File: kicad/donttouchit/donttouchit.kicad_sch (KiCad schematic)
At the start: 46 parts, among them J1 Conn_01x02_Female, J10 Conn_01x04_Male, J2 Conn_01x02_Female, J3 Conn_01x02_Female, J4 Conn_01x02_Female, J5 Conn_01x02_Female, J6 Conn_01x02_Female, J7 Conn_01x02_Female, J8 Conn_01x02_Female, J9 Conn_01x02_Female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

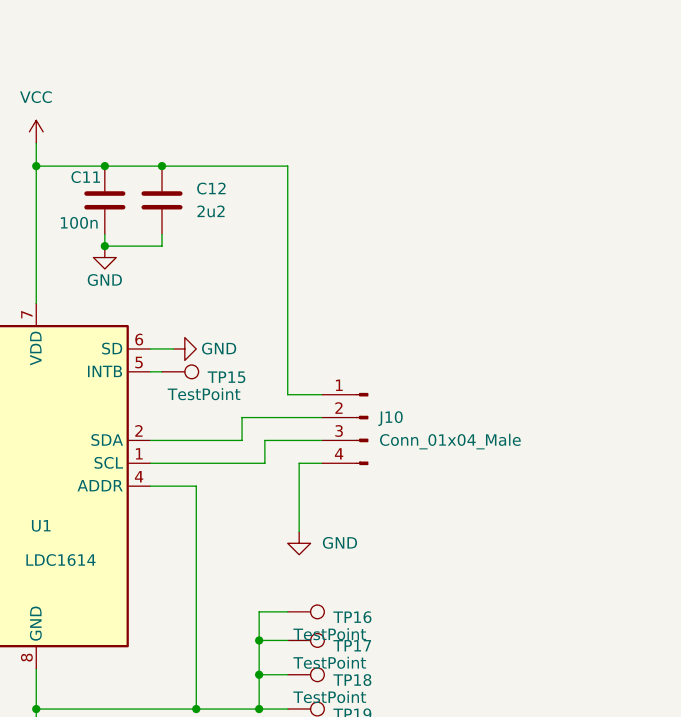
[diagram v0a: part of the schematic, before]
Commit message: i2c pull up resistors added
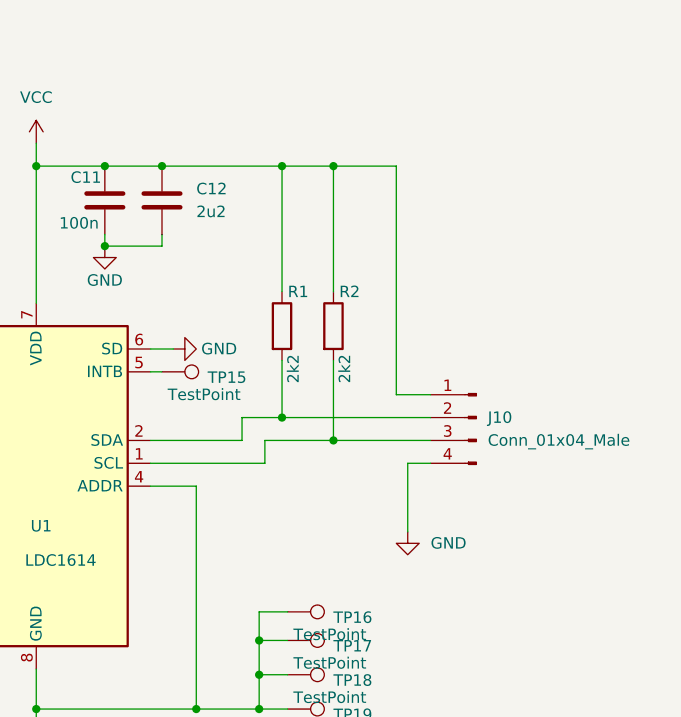
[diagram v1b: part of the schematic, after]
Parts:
- added R1, R2: 2k2, Resistor_SMD:R_0603_1608Metric_Pad0.98x0.95mm_HandSolder, symbol Device:R
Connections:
- net VCC: now also R1.1, R2.1
- net at J10.3 (Pin_3), U1.1 (SCL): now also R2.2
- net at J10.2 (Pin_2), U1.2 (SDA): now also R1.2
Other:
- moved on the sheet: J10
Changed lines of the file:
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@@
   (junction (at 57.785 93.98) (diameter 0) (color 0 0 0 0)
   )
+  (junction (at 204.47 75.565) (diameter 0) (color 0 0 0 0)
+  )
   (junction (at 57.785 115.57) (diameter 0) (color 0 0 0 0)
   )
+  (junction (at 198.755 75.565) (diameter 0) (color 0 0 0 0)
+  )
   (junction (at 57.785 104.775) (diameter 0) (color 0 0 0 0)
   )
@@
   (junction (at 134.62 100.965) (diameter 0) (color 0 0 0 0)
   )
+  (junction (at 198.755 103.505) (diameter 0) (color 0 0 0 0)
+  )
   (junction (at 107.95 103.505) (diameter 0) (color 0 0 0 0)
   )
@@
   (junction (at 179.07 84.455) (diameter 0) (color 0 0 0 0)
   )
+  (junction (at 204.47 106.045) (diameter 0) (color 0 0 0 0)
+  )
   (wire (pts (xy 93.345 110.49) (xy 93.345 113.665))
     (stroke (width 0) (type default) (color 0 0 0 0))
@@
     (stroke (width 0) (type default) (color 0 0 0 0))
   )
+  (wire (pts (xy 198.755 75.565) (xy 204.47 75.565))
+    (stroke (width 0) (type default) (color 0 0 0 0))
+  )
   (wire (pts (xy 196.215 132.08) (xy 196.215 135.89))
     (stroke (width 0) (type default) (color 0 0 0 0))
@@
     (stroke (width 0) (type default) (color 0 0 0 0))
   )
+  (wire (pts (xy 204.47 97.155) (xy 204.47 106.045))
+    (stroke (width 0) (type default) (color 0 0 0 0))
+  )
   (wire (pts (xy 50.8 115.57) (xy 50.8 116.205))
     (stroke (width 0) (type default) (color 0 0 0 0))
@@
     (stroke (width 0) (type default) (color 0 0 0 0))
   )
-  (wire (pts (xy 194.31 103.505) (xy 203.2 103.505))
+  (wire (pts (xy 194.31 103.505) (xy 198.755 103.505))
     (stroke (width 0) (type default) (color 0 0 0 0))
   )
@@
     (stroke (width 0) (type default) (color 0 0 0 0))
   )
-  (wire (pts (xy 199.39 75.565) (xy 199.39 100.965))
+  (wire (pts (xy 211.455 75.565) (xy 211.455 100.965))
     (stroke (width 0) (type default) (color 0 0 0 0))
   )
@@
     (stroke (width 0) (type default) (color 0 0 0 0))
   )
-  (wire (pts (xy 199.39 100.965) (xy 203.2 100.965))
+  (wire (pts (xy 211.455 100.965) (xy 215.265 100.965))
     (stroke (width 0) (type default) (color 0 0 0 0))
   )
@@
     (stroke (width 0) (type default) (color 0 0 0 0))
   )
-  (wire (pts (xy 203.2 108.585) (xy 200.66 108.585))
+  (wire (pts (xy 215.265 108.585) (xy 212.725 108.585))
     (stroke (width 0) (type default) (color 0 0 0 0))
   )
@@
     (stroke (width 0) (type default) (color 0 0 0 0))
   )
+  (wire (pts (xy 198.755 75.565) (xy 198.755 89.535))
+    (stroke (width 0) (type default) (color 0 0 0 0))
+  )
   (wire (pts (xy 73.025 100.33) (xy 73.025 103.505))
     (stroke (width 0) (type default) (color 0 0 0 0))
   )
-  (wire (pts (xy 185.42 75.565) (xy 199.39 75.565))
+  (wire (pts (xy 198.755 97.155) (xy 198.755 103.505))
     (stroke (width 0) (type default) (color 0 0 0 0))
   )
@@
     (stroke (width 0) (type default) (color 0 0 0 0))
   )
+  (wire (pts (xy 204.47 75.565) (xy 204.47 89.535))
+    (stroke (width 0) (type default) (color 0 0 0 0))
+  )
   (wire (pts (xy 134.62 56.515) (xy 139.7 56.515))
     (stroke (width 0) (type default) (color 0 0 0 0))
@@
     (stroke (width 0) (type default) (color 0 0 0 0))
   )
+  (wire (pts (xy 204.47 106.045) (xy 215.265 106.045))
+    (stroke (width 0) (type default) (color 0 0 0 0))
+  )
   (wire (pts (xy 100.965 93.98) (xy 100.965 97.155))
     (stroke (width 0) (type default) (color 0 0 0 0))
@@
     (stroke (width 0) (type default) (color 0 0 0 0))
   )
+  (wire (pts (xy 204.47 75.565) (xy 211.455 75.565))
+    (stroke (width 0) (type default) (color 0 0 0 0))
+  )
   (wire (pts (xy 82.55 115.57) (xy 73.66 115.57))
     (stroke (width 0) (type default) (color 0 0 0 0))
@@
     (stroke (width 0) (type default) (color 0 0 0 0))
   )
+  (wire (pts (xy 198.755 103.505) (xy 215.265 103.505))
+    (stroke (width 0) (type default) (color 0 0 0 0))
+  )
   (wire (pts (xy 107.315 121.285) (xy 107.315 124.46))
     (stroke (width 0) (type default) (color 0 0 0 0))
@@
     (stroke (width 0) (type default) (color 0 0 0 0))
   )
+  (wire (pts (xy 185.42 75.565) (xy 198.755 75.565))
+    (stroke (width 0) (type default) (color 0 0 0 0))
+  )
   (wire (pts (xy 140.97 118.745) (xy 144.78 118.745))
     (stroke (width 0) (type default) (color 0 0 0 0))
@@
     (stroke (width 0) (type default) (color 0 0 0 0))
   )
-  (wire (pts (xy 200.66 108.585) (xy 200.66 116.205))
+  (wire (pts (xy 212.725 108.585) (xy 212.725 116.205))
     (stroke (width 0) (type default) (color 0 0 0 0))
   )
@@
     (stroke (width 0) (type default) (color 0 0 0 0))
   )
-  (wire (pts (xy 196.85 106.045) (xy 203.2 106.045))
+  (wire (pts (xy 196.85 106.045) (xy 204.47 106.045))
     (stroke (width 0) (type default) (color 0 0 0 0))
   )
@@
     (pin "1")
   )
+  (symbol (lib_id "Device:R") (at 198.755 93.345 0) (unit 1)
+    (in_bom yes) (on_board yes)
+    (property "Reference" "R1" (id 0) (at 199.39 89.535 0)
+      (effects (font (size 1.27 1.27)) (justify left))
+    )
+    (property "Value" "2k2" (id 1) (at 200.025 99.695 90)
+      (effects (font (size 1.27 1.27)) (justify left))
+    )
+    (property "Footprint" "Resistor_SMD:R_0603_1608Metric_Pad0.98x0.95mm_HandSolder" (id 2) (at 196.977 93.345 90)
+      (effects (font (size 1.27 1.27)) hide)
+    )
+    (property "Datasheet" "~" (id 3) (at 198.755 93.345 0)
+      (effects (font (size 1.27 1.27)) hide)
+    )
+    (pin "1")
+    (pin "2")
+  )
   (symbol (lib_id "Connector:TestPoint") (at 185.42 98.425 270) (unit 1)
     (in_bom yes) (on_board yes)
@@
     (pin "2")
   )
-  (symbol (lib_id "power:GND") (at 200.66 116.205 0) (mirror y) (unit 1)
-    (in_bom yes) (on_board yes) (fields_autoplaced)
-    (property "Reference" "#PWR09" (id 0) (at 200.66 122.555 0)
-      (effects (font (size 1.27 1.27)) hide)
-    )
-    (property "Value" "GND" (id 1) (at 203.2 117.4749 0)
+  (symbol (lib_id "power:GND") (at 212.725 116.205 0) (mirror y) (unit 1)
+    (in_bom yes) (on_board yes) (fields_autoplaced)
+    (property "Reference" "#PWR09" (id 0) (at 212.725 122.555 0)
+      (effects (font (size 1.27 1.27)) hide)
+    )
+    (property "Value" "GND" (id 1) (at 215.265 117.4749 0)
       (effects (font (size 1.27 1.27)) (justify right))
     )
-    (property "Footprint" "" (id 2) (at 200.66 116.205 0)
-      (effects (font (size 1.27 1.27)) hide)
-    )
-    (property "Datasheet" "" (id 3) (at 200.66 116.205 0)
+    (property "Footprint" "" (id 2) (at 212.725 116.205 0)
+      (effects (font (size 1.27 1.27)) hide)
+    )
+    (property "Datasheet" "" (id 3) (at 212.725 116.205 0)
       (effects (font (size 1.27 1.27)) hide)
     )
@@
     (pin "1")
   )
-  (symbol (lib_id "Connector:Conn_01x04_Male") (at 208.28 103.505 0) (mirror y) (unit 1)
-    (in_bom yes) (on_board yes) (fields_autoplaced)
-    (property "Reference" "J10" (id 0) (at 209.55 103.5049 0)
+  (symbol (lib_id "Connector:Conn_01x04_Male") (at 220.345 103.505 0) (mirror y) (unit 1)
+    (in_bom yes) (on_board yes) (fields_autoplaced)
+    (property "Reference" "J10" (id 0) (at 221.615 103.5049 0)
       (effects (font (size 1.27 1.27)) (justify right))
     )
-    (property "Value" "Conn_01x04_Male" (id 1) (at 209.55 106.0449 0)
+    (property "Value" "Conn_01x04_Male" (id 1) (at 221.615 106.0449 0)
       (effects (font (size 1.27 1.27)) (justify right))
     )
-    (property "Footprint" "Connector_JST:JST_PH_B4B-PH-SM4-TB_1x04-1MP_P2.00mm_Vertical" (id 2) (at 208.28 103.505 0)
-      (effects (font (size 1.27 1.27)) hide)
-    )
-    (property "Datasheet" "~" (id 3) (at 208.28 103.505 0)
+    (property "Footprint" "Connector_JST:JST_PH_B4B-PH-SM4-TB_1x04-1MP_P2.00mm_Vertical" (id 2) (at 220.345 103.505 0)
+      (effects (font (size 1.27 1.27)) hide)
+    )
+    (property "Datasheet" "~" (id 3) (at 220.345 103.505 0)
       (effects (font (size 1.27 1.27)) hide)
     )
@@
     (pin "1")
   )
+  (symbol (lib_id "Device:R") (at 204.47 93.345 0) (unit 1)
+    (in_bom yes) (on_board yes)
+    (property "Reference" "R2" (id 0) (at 205.105 89.535 0)
+      (effects (font (size 1.27 1.27)) (justify left))
+    )
+    (property "Value" "2k2" (id 1) (at 205.74 99.695 90)
+      (effects (font (size 1.27 1.27)) (justify left))
+    )
+    (property "Footprint" "Resistor_SMD:R_0603_1608Metric_Pad0.98x0.95mm_HandSolder" (id 2) (at 202.692 93.345 90)
+      (effects (font (size 1.27 1.27)) hide)
+    )
+    (property "Datasheet" "~" (id 3) (at 204.47 93.345 0)
+      (effects (font (size 1.27 1.27)) hide)
+    )
+    (pin "1")
+    (pin "2")
+  )
   (symbol (lib_id "power:GND") (at 134.62 85.725 0) (unit 1)
     (in_bom yes) (on_board yes) (fields_autoplaced)
@@
       (reference "L3") (unit 1) (value "PCB Coil") (footprint "Library:Coil")
     )
+    (path "/39624e1f-8c52-44d2-9675-d08e055559ed"
+      (reference "R1") (unit 1) (value "2k2") (footprint "Resistor_SMD:R_0603_1608Metric_Pad0.98x0.95mm_HandSolder")
+    )
+    (path "/f0806e7c-4b6c-4326-bfd0-53fcb69c9d00"
+      (reference "R2") (unit 1) (value "2k2") (footprint "Resistor_SMD:R_0603_1608Metric_Pad0.98x0.95mm_HandSolder")
+    )
     (path "/ea8f5060-c83f-4b39-9e48-2e7638c5ee62"

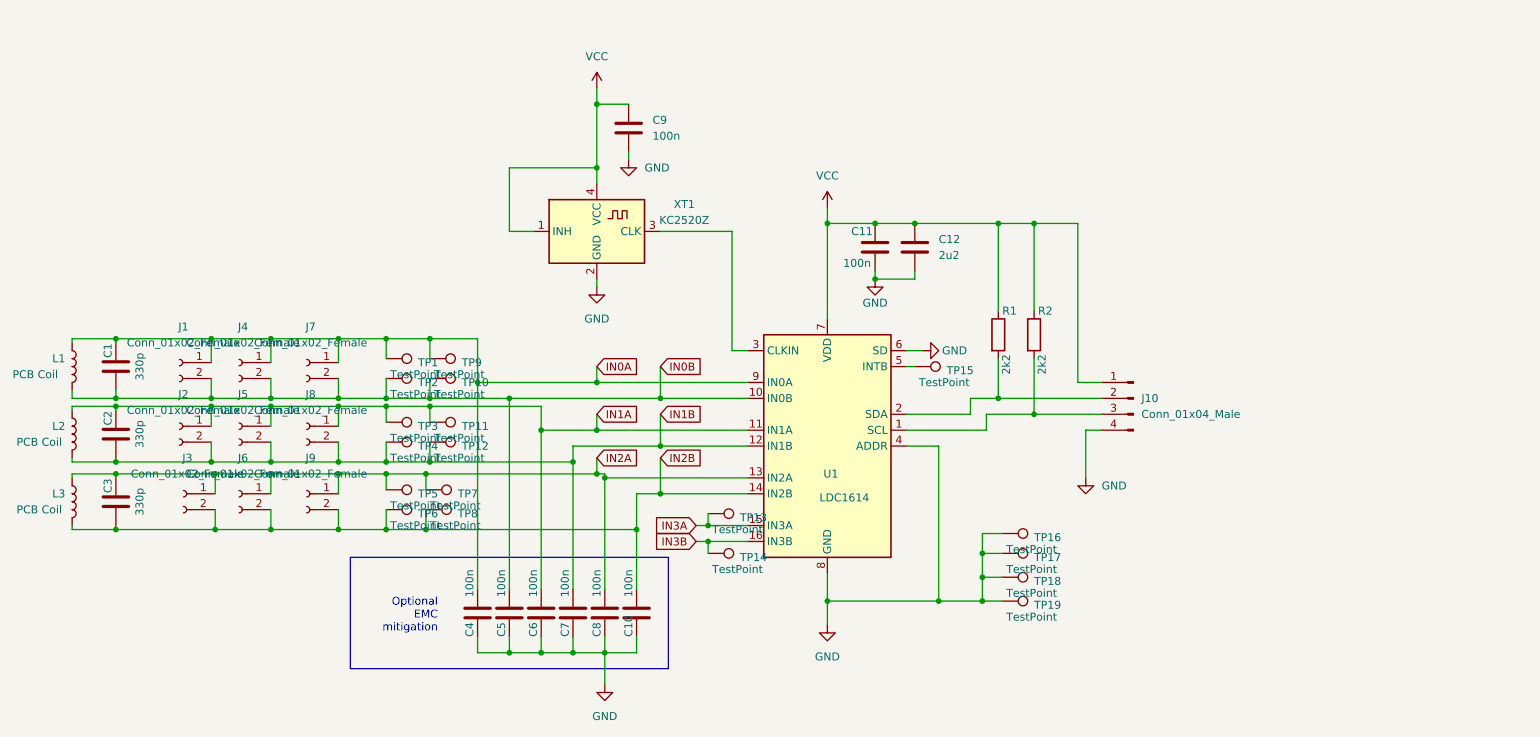
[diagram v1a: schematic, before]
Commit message: temperature sensor added
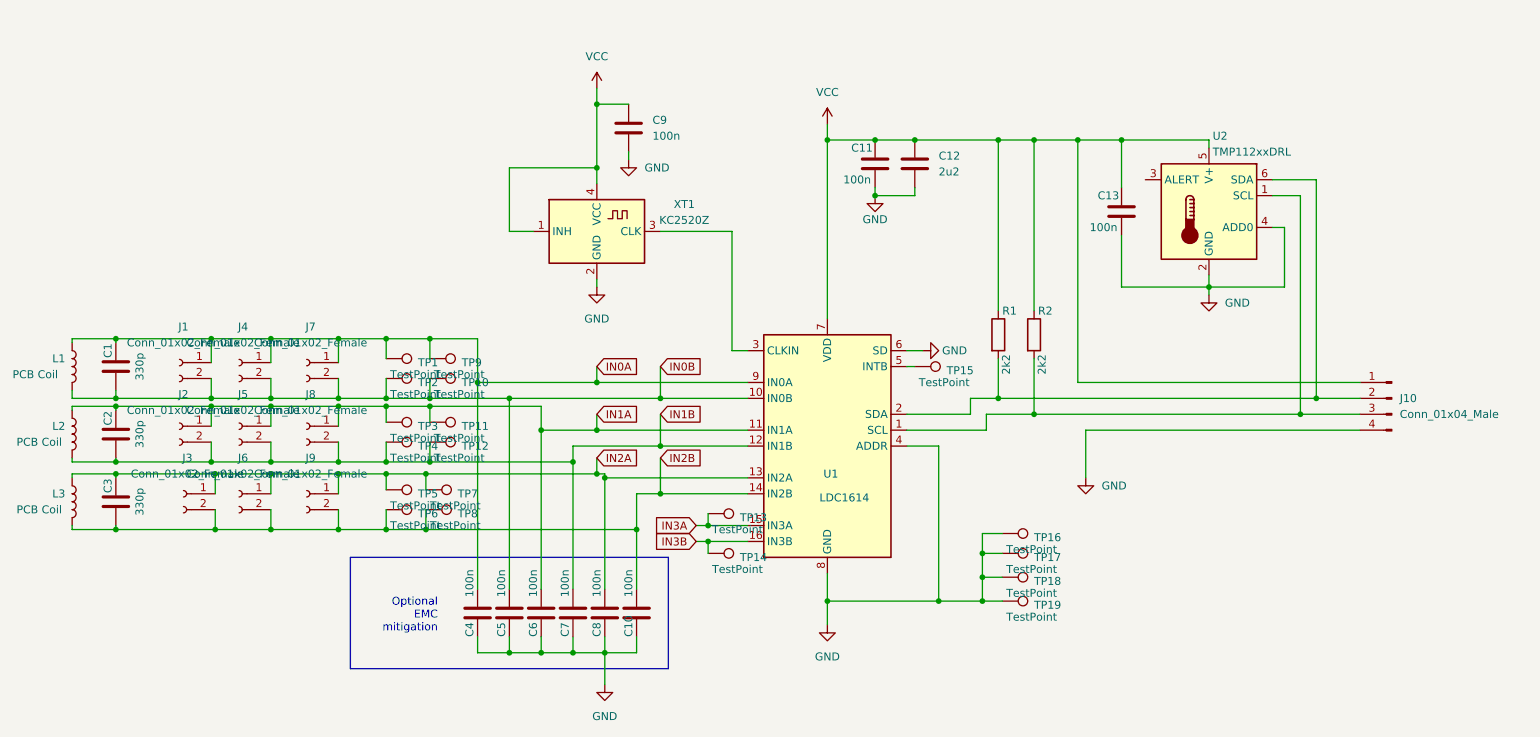
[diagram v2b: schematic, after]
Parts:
- added C13: 100n, Capacitor_SMD:C_0603_1608Metric_Pad1.08x0.95mm_HandSolder, symbol Device:C
- added U2: TMP112xxDRL, Package_TO_SOT_SMD:SOT-563, symbol Sensor_Temperature:TMP112xxDRL
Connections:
- net GND: now also C13.2, U2.2 (GND), U2.4 (ADD0)
- net VCC: now also C13.1, U2.5 (V+)
- net at J10.3 (Pin_3), R2.2, U1.1 (SCL): now also U2.1 (SCL)
- net at J10.2 (Pin_2), R1.2, U1.2 (SDA): now also U2.6 (SDA)
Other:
- moved on the sheet: C11, C12, J10

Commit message: I2C address solderbridges added / mounting hole added / size reduced for control section
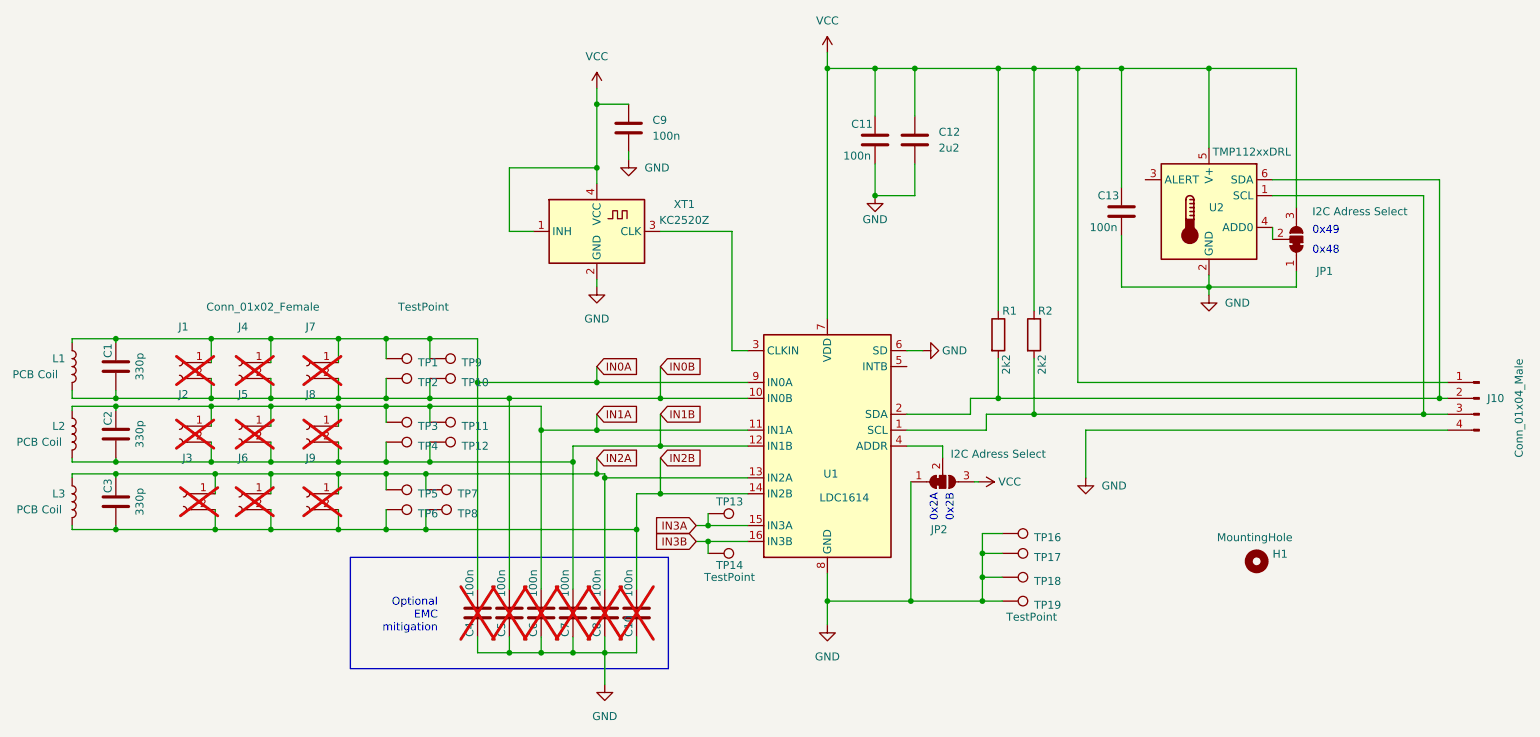
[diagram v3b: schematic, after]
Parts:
- removed TP15: TestPoint, TestPoint:TestPoint_THTPad_1.5x1.5mm_Drill0.7mm, symbol Connector:TestPoint
- added H1: MountingHole, MountingHole:MountingHole_3.2mm_M3, symbol Mechanical:MountingHole
- added JP1, JP2: I2C Adress Select, Jumper:SolderJumper-3_P1.3mm_Bridged12_RoundedPad1.0x1.5mm, symbol Jumper:SolderJumper_3_Bridged12
- C10, C4, C5, C6, C7, C8, J1, J2, J3, J4, J5, J6, J7, J8, J9: now not fitted
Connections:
- net GND: now also JP1.1 (A), JP2.1 (A); no longer U1.4 (ADDR), U2.4 (ADD0)
- net VCC: now also JP1.3 (B), JP2.3 (B)
- new net: JP2.2 (C), U1.4 (ADDR)
- new net: JP1.2 (C), U2.4 (ADD0)
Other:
- note added: "0x2A"
- note added: "0x2B"
- note added: "0x48"
- note added: "0x49"
- moved on the sheet: C11, C12, J10
